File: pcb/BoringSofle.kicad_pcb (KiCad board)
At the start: 2 copper layers, 138.2 x 110 mm, 75 parts

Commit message: update kicad project pcbs
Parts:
- removed REF**: boring_sofle_text, BoringSofle:boring_sofle_text
- removed REF**: logo_v1_big, BoringSofle:logo_v1_big
- moved RE1 3.80 mm to (262.9, 162.0), turned to 270 degrees
- moved SW1 3.80 mm to (262.9, 162.0), turned to 180 degrees
- moved JST1 2.80 mm to (254.9, 145.1)
- moved H1 0.60 mm to (254.9, 153.1)
- moved H2 0.60 mm to (270.9, 153.1)
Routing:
- net (no net): track 0.00 -> 1027.9 mm, vias 0 -> 21
- net P19: track 272.2 -> 135.2 mm, vias 7 -> 6
- net P18: track 256.0 -> 133.8 mm, vias 7 -> 6
- net P15: track 241.4 -> 137.2 mm, vias 7 -> 6
- net P14: track 225.9 -> 138.5 mm, vias 7 -> 6
- net P16: track 209.6 -> 138.8 mm, vias 7 -> 6
- net P5: track 179.4 -> 109.0 mm, vias 6 -> 5
- net P6: track 175.1 -> 109.0 mm, vias 6 -> 5
- net P7: track 169.9 -> 109.0 mm, vias 6 -> 5
- net CS: track 60.5 -> 0.00 mm, vias 1 -> 0
- net RST: track 59.0 -> 0.00 mm, vias 2 -> 0
- net P9: track 153.1 -> 94.5 mm
- net P10: track 137.9 -> 83.0 mm, vias 5 -> 4
- net RAW: track 54.0 -> 0.00 mm, vias 2 -> 0
- net P3: track 50.5 -> 0.00 mm, vias 1 -> 0
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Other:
- board text removed: "JLCJLCJLCJLC"

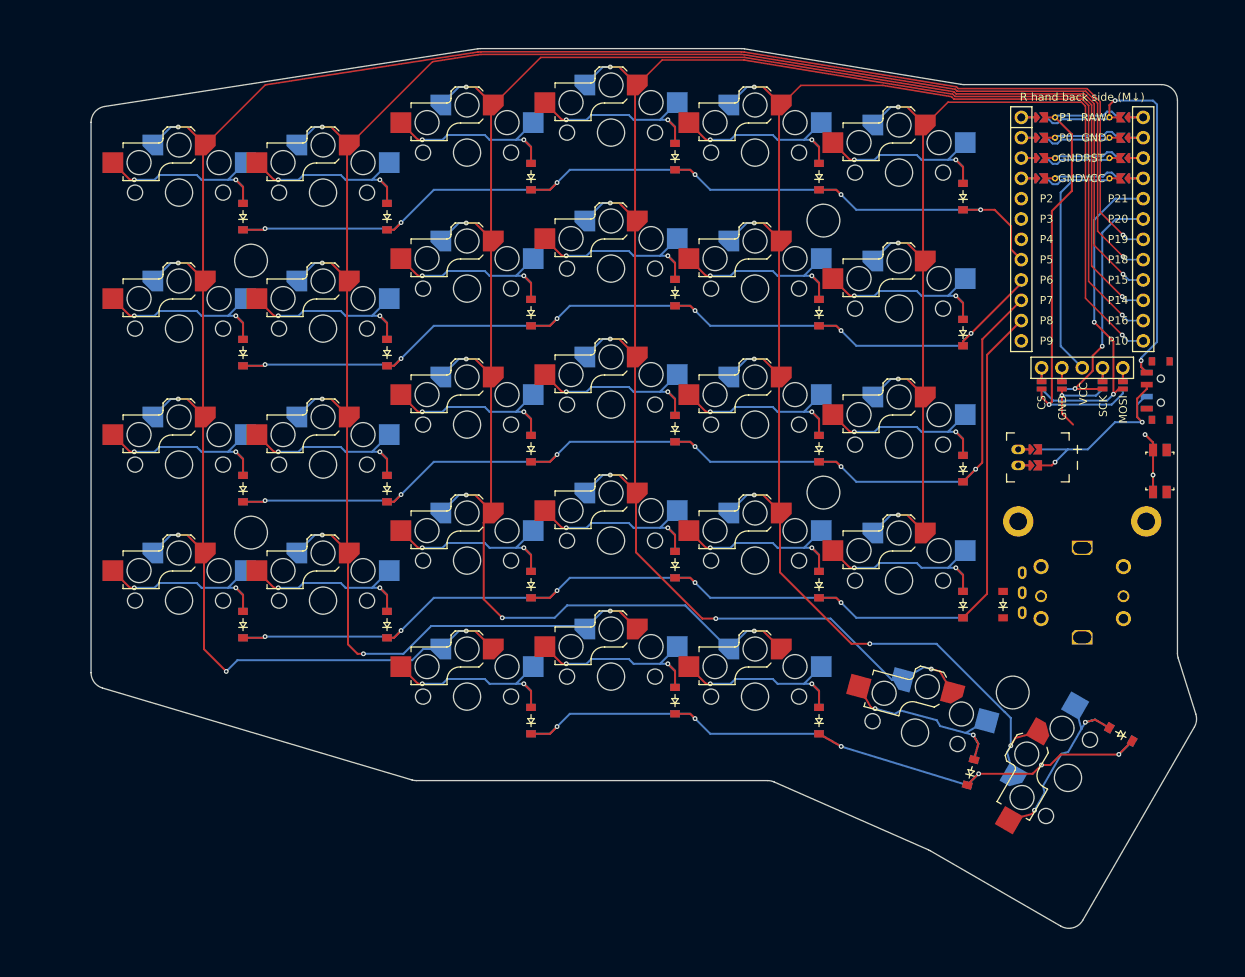
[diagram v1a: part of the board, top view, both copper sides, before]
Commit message: shift encoder position and rotation, redesign top plate
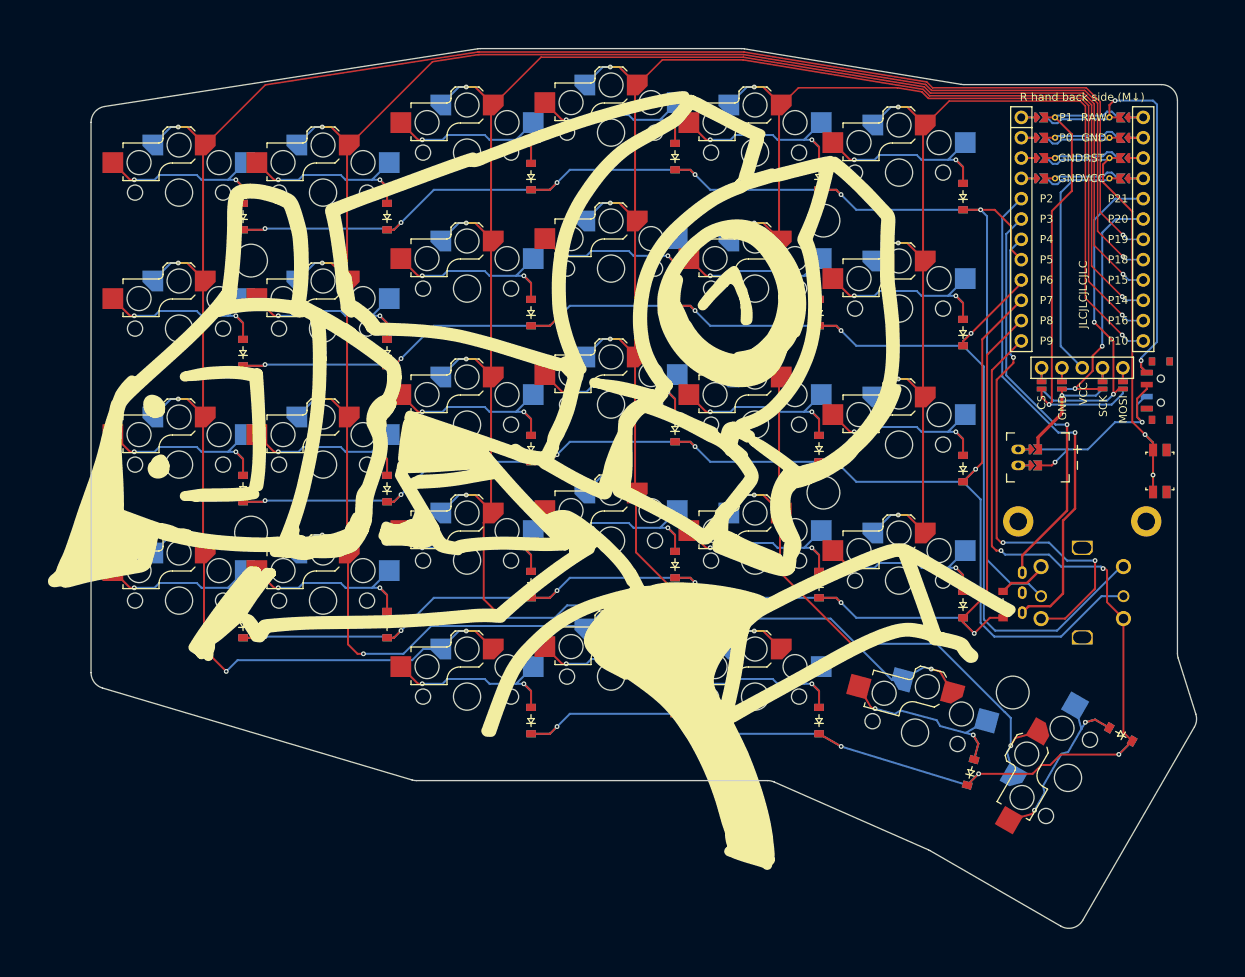
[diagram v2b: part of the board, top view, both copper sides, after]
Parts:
- added REF**: logo_v1_big, BoringSofle:logo_v1_big, F.Cu at (189.0, 197.4)
- added REF**: boring_sofle_text, BoringSofle:boring_sofle_text, F.Cu at (166.9, 177.6)
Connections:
- H1 pad : (no net) -> GND
- H2 pad : (no net) -> GND
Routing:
- net (no net): track 1027.9 -> 0.00 mm, vias 21 -> 0
- net P19: track 135.2 -> 272.4 mm, vias 6 -> 7
- net P18: track 133.8 -> 256.2 mm, vias 6 -> 7
- net P15: track 137.2 -> 241.6 mm, vias 6 -> 7
- net P14: track 138.5 -> 226.1 mm, vias 6 -> 7
- net P16: track 138.8 -> 209.7 mm, vias 6 -> 7
- net P6: track 109.0 -> 178.4 mm, vias 5 -> 6
- net P7: track 109.0 -> 176.1 mm, vias 5 -> 6
- net P5: track 109.0 -> 175.4 mm, vias 5 -> 6
- net P9: track 94.5 -> 159.9 mm, vias 6 -> 7
- net P4: track 0.00 -> 64.2 mm, vias 0 -> 3
- net P2: track 0.00 -> 62.0 mm, vias 0 -> 1
- net CS: track 0.00 -> 60.5 mm, vias 0 -> 1
- net RST: track 0.00 -> 59.0 mm, vias 0 -> 2
- net P10: track 83.0 -> 138.0 mm, vias 4 -> 5
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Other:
- board text added: "JLCJLCJLCJLC"
